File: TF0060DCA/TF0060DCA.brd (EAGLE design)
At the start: 53.3 x 20.7 mm, 18 parts, among them IC1 LM1972MX_NOPB, IC2 7805T, IC8 LM1117MPX-3.3

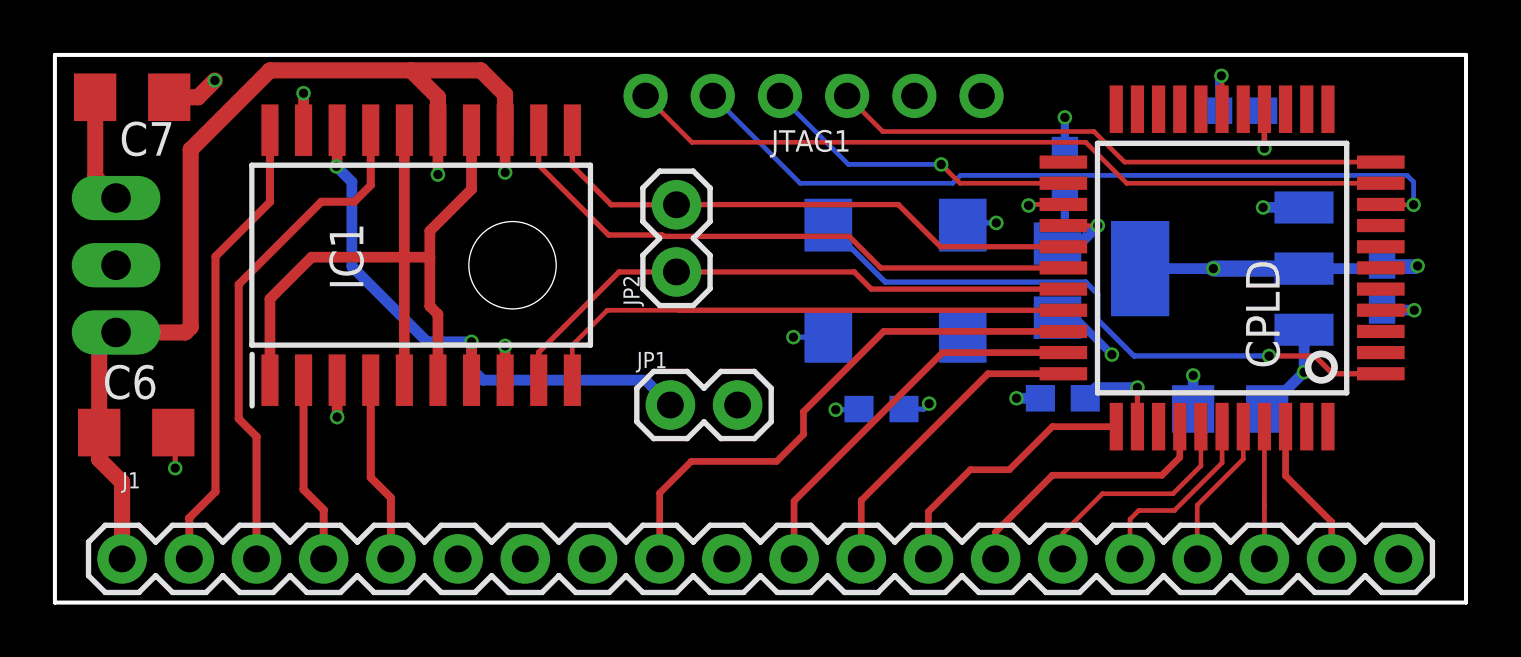
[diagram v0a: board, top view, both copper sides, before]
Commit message: upgraded the DC bias
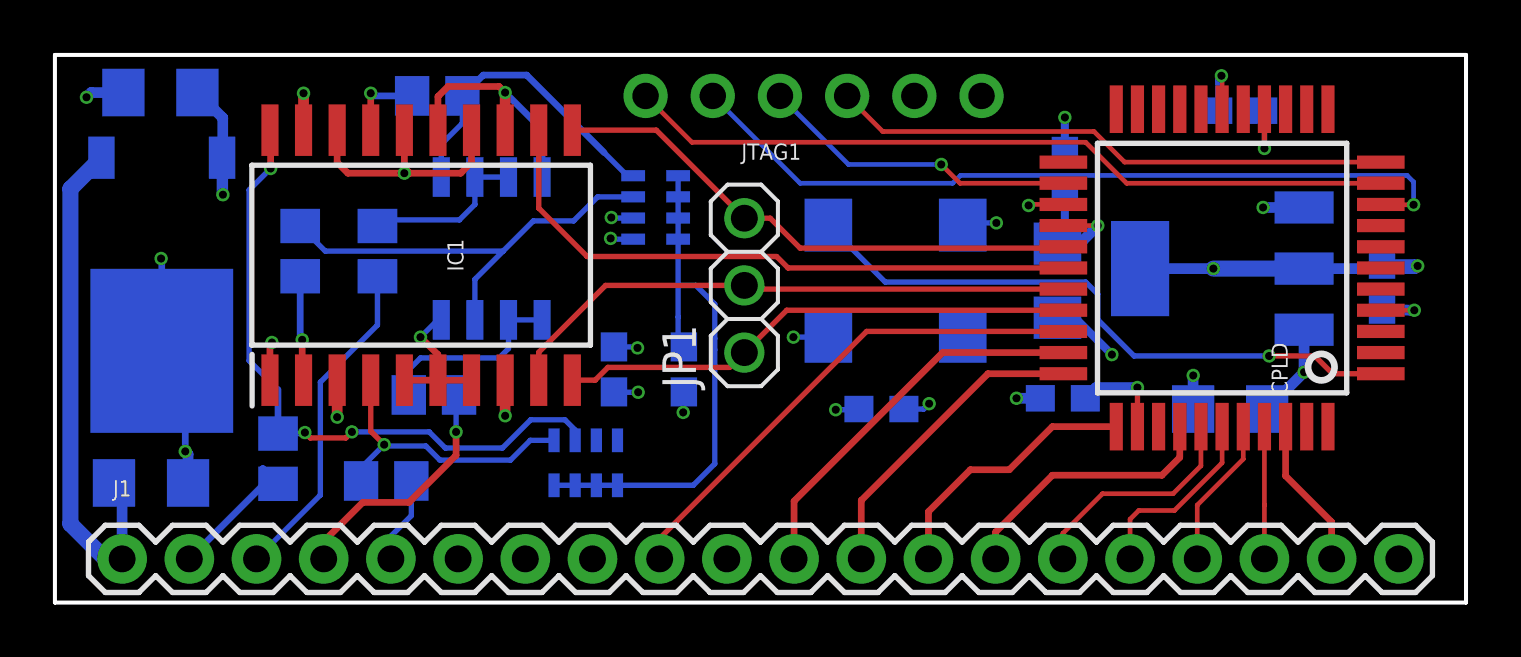
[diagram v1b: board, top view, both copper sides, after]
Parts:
- removed JP2: (no value), SparkFun-Retired:1X02
- added C10, C11, C14, C15, C8, C9: 6uF, rcl:C0805
- added C17: 1uF, eagle-ltspice:C0603
- added C18: 100nF, eagle-ltspice:C0603
- added IC12: MCP6002T-I_SN, MCP6002T-I_SN:SOIC127P600X175-8N
- added RN3, RN4: CAY16-104J4LF, CAY16-103J4LF:RESCAXE80P320X160-8N
- C6, C7: value (none) -> 10uF
- IC2: value 7805T -> 7805DT; device linear:TO220H -> linear:TO252
- JP1: device SparkFun-Retired:1X02 -> adafruit:1X03
- OSC2: value X100MHZ -> 25MHZ
- moved IC2 8.46 mm to (4.04, 12.9), turned to 180 degrees
- moved JP1 5.31 mm to (26.1, 12.9), turned to 90 degrees
- moved C6 1.99 mm to (3.63, 5.41), flipped to the bottom, turned to 180 degrees
- moved C7 1.08 mm to (3.99, 20.2), flipped to the bottom
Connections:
- removed net AGND: IC1.1, IC1.14, IC1.16, IC1.5, IC1.6
- removed net VSS: IC1.18, IC1.7, JP1.1
- new net ATNOUTRAW1: C9.2, IC1.2
- new net ATNOUTRAW2: C10.2, IC1.17
- new net BUFFER_IN1: C9.1, IC12.3, RN3.3
- new net BUFFER_IN2: C10.1, IC12.5, RN3.4
- new net INBIAS1: C11.1, IC1.4, RN4.1
- new net INBIAS2: C8.1, IC1.20, RN4.2
- new net NC: J1.8
- new net OUTB1: C14.1, IC12.1, IC12.2
- new net OUTB2: C15.1, IC12.6, IC12.7
- new net VBIAS: C18.1, RN3.5, RN3.6, RN3.7, RN3.8, RN4.5, RN4.6, RN4.7, RN4.8
- net DI: now also JP1.3; no longer JP2.2
- net GND: now also C17.2, C18.2, IC1.1, IC1.14, IC1.16, IC1.18, IC1.5, IC1.6, IC1.7, IC12.4, IC2.3, RN3.2; no longer IC2.2, JP1.2
- net IN1: now also C11.2; no longer IC1.4
- net IN2: now also C8.2; no longer IC1.20
- net LOAD_SHIFT: now also JP1.1
- net OUT1: now also C14.2; no longer IC1.2
- net OUT2: now also C15.2; no longer IC1.17
- net SCLK: now also JP1.2; no longer JP2.1
- net VCC: now also C17.1, IC2.2, RN3.1; no longer IC2.3, J1.8
- net VDD: now also IC12.8
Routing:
- net AGND: track 29.5 -> 0.00 mm
- net GND: track 23.8 -> 50.0 mm, vias 15 -> 22
- net INBIAS2: track 0.00 -> 24.9 mm, vias 0 -> 3
- net VSS: track 22.3 -> 0.00 mm, vias 2 -> 0
- net VBIAS: track 0.00 -> 20.7 mm
- net BUFFER_IN1: track 0.00 -> 16.9 mm
- net IN2: track 17.5 -> 5.38 mm
- net BUFFER_IN2: track 0.00 -> 11.8 mm
- net INBIAS1: track 0.00 -> 11.4 mm, vias 0 -> 1
- net VDD: track 39.9 -> 29.1 mm, vias 2 -> 1
- net OUTB1: track 0.00 -> 7.41 mm
- net OUT2: track 19.3 -> 12.6 mm
- net OUTB2: track 0.00 -> 6.33 mm
- net ATNOUTRAW1: track 0.00 -> 3.98 mm, vias 0 -> 1
- net IN1: track 7.07 -> 3.27 mm
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- added copper zone on layer 2, net VDD

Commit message: Updated to CH32 control chip
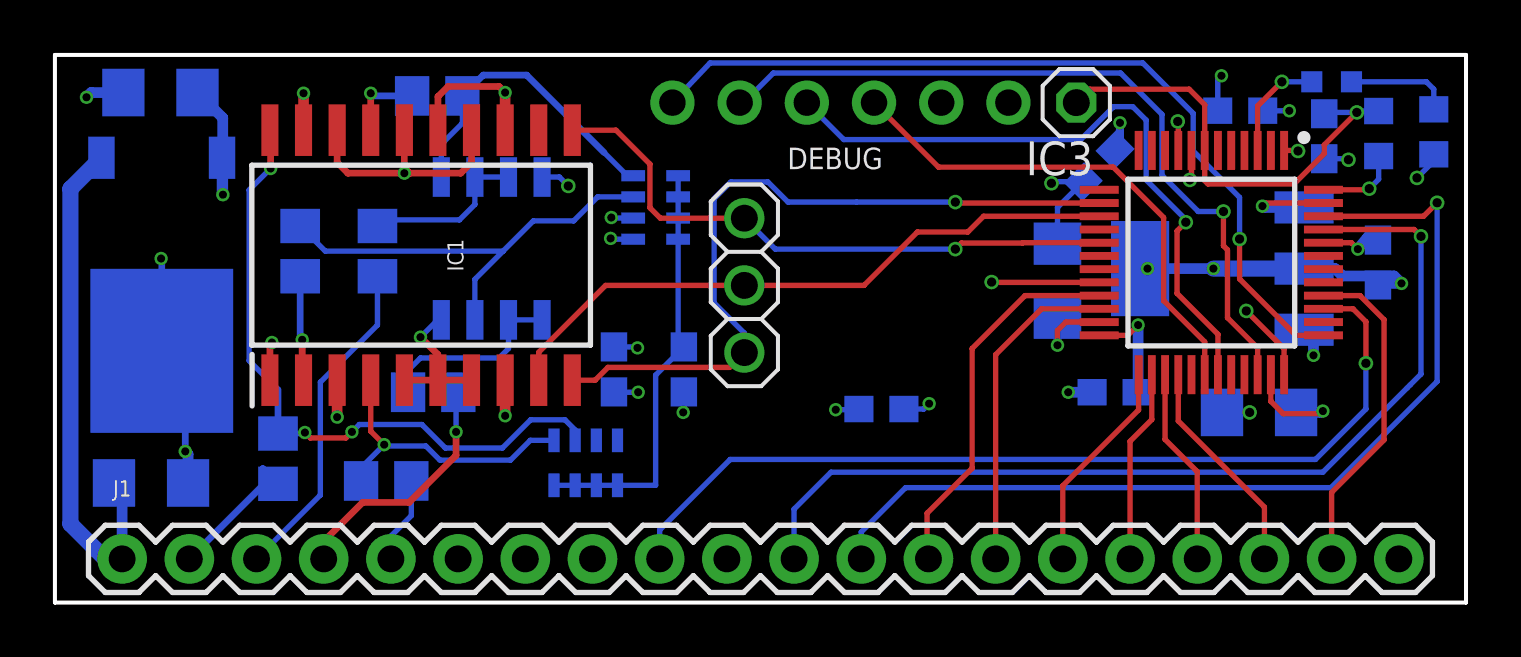
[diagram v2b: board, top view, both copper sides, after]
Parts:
- removed CPLD: XC9536XL-10VQ44C, xilinx-xc9:SQFP-S-10X10-44
- removed JTAG1: JTAG, microbuilder:1X06_ROUND
- removed OSC2: 25MHZ, microbuilder:OSC_7X5MM
- added C12: 0.1uF, eagle-ltspice:C0603
- added DEBUG: JTAG, microbuilder:1X06_ROUND
- added IC3: CH32V203C, SamacSys_Parts:QFP50P900X900X160-48N
- added JP2: (no value), pinhead:1X01
- added LED1: (no value), adafruit:CHIPLED_0603
- added R1: 2K2, resistor:R0603
- added R2: 100K, resistor:R0603
- moved C4 1.97 mm to (40.1, 8.84)
- moved C2 1.33 mm to (39.5, 17.4), turned to 135 degrees
- moved C1 1.10 mm to (45.5, 8.08), turned to 180 degrees
- moved C5 0.93 mm to (50.0, 13.7), turned to 90 degrees
- moved C14 0.10 mm to (14.3, 8.84)
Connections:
- removed net CLKOUT: CPLD.1, OSC2.3
- removed net DO: CPLD.28, IC1.12
- removed net TCK: CPLD.11, JTAG1.4
- removed net TDI: CPLD.9, JTAG1.2
- removed net TDO: CPLD.24, JTAG1.3
- removed net TMS: CPLD.10, JTAG1.1
- new net N$3: IC3.3, LED1.C
- new net N$4: LED1.A, R1.2
- new net NRST: C12.1, IC3.7, JP2.1, R2.2
- new net RX: DEBUG.3, IC3.31
- new net SWCLK: DEBUG.1, IC3.37
- new net SWDIO: DEBUG.2, IC3.34
- new net TX: DEBUG.4, IC3.30
- net CLK1: now also IC3.39; no longer CPLD.31
- net CLK2: now also IC3.40; no longer CPLD.42
- net DI: now also IC3.17; no longer CPLD.27
- net GND: now also C12.2, DEBUG.5, IC3.20, IC3.23, IC3.35, IC3.44, IC3.47, IC3.8; no longer CPLD.17, CPLD.25, CPLD.4, JTAG1.5, OSC2.2
- net LOAD_SHIFT: now also IC3.14; no longer CPLD.30
- net SCLK: now also IC3.15; no longer CPLD.29
- net SD0: now also IC3.45; no longer CPLD.32
- net SD1: now also IC3.46; no longer CPLD.33
- net SD2: now also IC3.21; no longer CPLD.34
- net SD3: now also IC3.22; no longer CPLD.37
- net SD4: now also IC3.25; no longer CPLD.38
- net SD5: now also IC3.26; no longer CPLD.39
- net SD6: now also IC3.27; no longer CPLD.40
- net SD7: now also IC3.28; no longer CPLD.41
- net VCC: now also IC12.8
- net VCC33: now also DEBUG.6, IC3.1, IC3.24, IC3.36, IC3.48, IC3.9, R1.1, R2.1; no longer CPLD.15, CPLD.26, CPLD.35, JTAG1.6, OSC2.4
- net VDD: no longer IC12.8
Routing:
- net SWCLK: track 0.00 -> 32.2 mm, vias 0 -> 1
- net TDI: track 30.2 -> 0.00 mm, vias 1 -> 0
- net TMS: track 29.2 -> 0.00 mm
- net SWDIO: track 0.00 -> 29.0 mm, vias 0 -> 1
- net RX: track 0.00 -> 25.2 mm, vias 0 -> 1
- net SD1: track 11.8 -> 36.4 mm, vias 0 -> 1
- net CLKOUT: track 23.8 -> 0.00 mm, vias 1 -> 0
- net DO: track 23.7 -> 0.00 mm
- net SD0: track 14.7 -> 36.7 mm, vias 0 -> 1
- net TCK: track 21.2 -> 0.00 mm
- net TX: track 0.00 -> 19.3 mm
- net NRST: track 0.00 -> 17.4 mm, vias 0 -> 1
- net CLK1: track 19.3 -> 34.8 mm, vias 0 -> 1
- net TDO: track 12.1 -> 0.00 mm, vias 1 -> 0
- net LOAD_SHIFT: track 19.7 -> 28.4 mm, vias 0 -> 1
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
